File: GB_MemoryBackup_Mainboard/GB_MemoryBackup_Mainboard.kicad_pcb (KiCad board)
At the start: 2 copper layers, 56.5 x 64.4 mm, 18 parts, among them J1 GB_Cart_EdgeConn-1Row-32Pins, J2 GB_Cart_Slot-1Row-32Pins, J3 JTAG-A, SW1 SW_SPDT, SW2 SW_Push, U1 AT29C010A-PLCC32, U2 28SF040-120-4C-NH-PLCC32, U3 Generic-ATF15xx-PLCC44

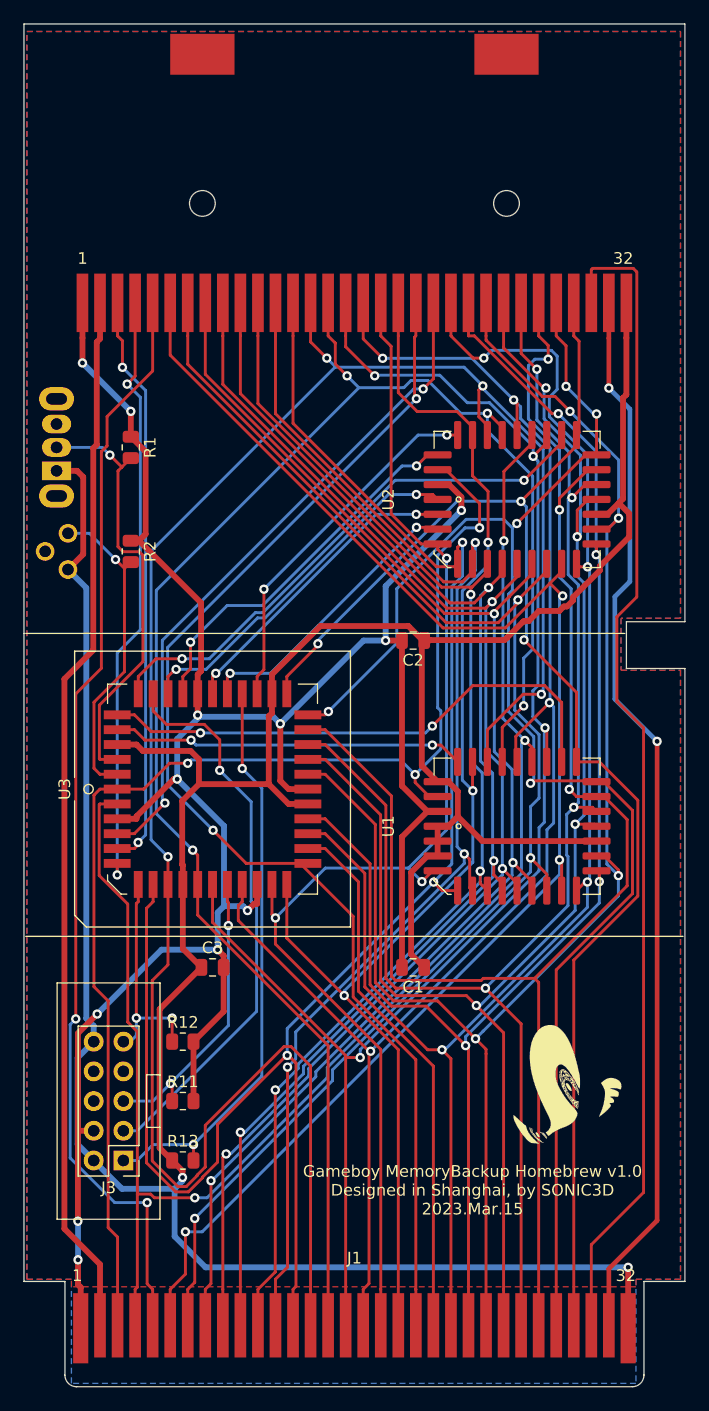
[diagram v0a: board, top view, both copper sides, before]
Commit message: Modified: PCB redesigned for using with plastic cart shell.
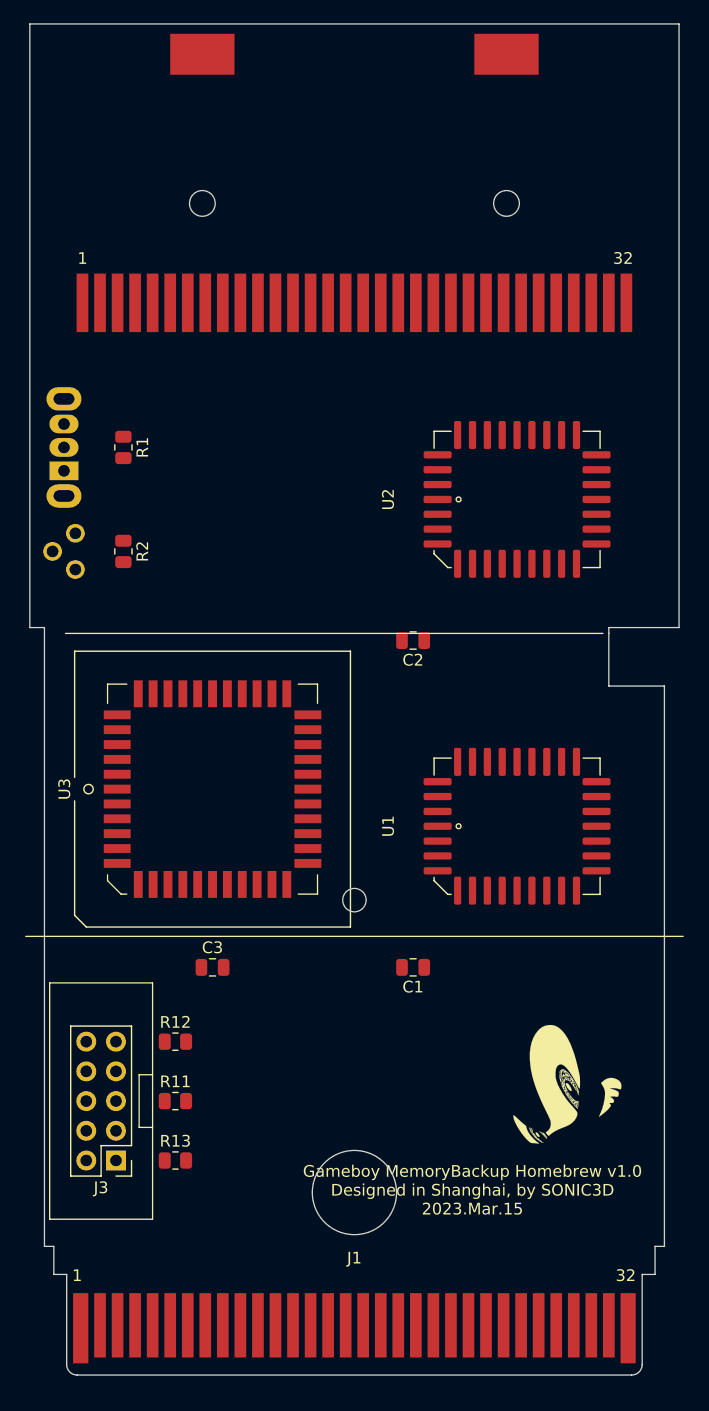
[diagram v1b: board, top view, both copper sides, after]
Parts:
- J1: footprint NintendoGBCart_ExtFootprint:GB_Cart_1x32_P1.50mm_Edge_For_RawPCB -> NintendoGBCart_ExtFootprint:GB_Cart_1x32_P1.50mm_Edge_For_CartShell
- moved R1 0.64 mm to (69.8, 76.2)
- moved R11 0.64 mm to (74.3, 132.1)
- moved R12 0.64 mm to (74.3, 127.0)
- moved R13 0.64 mm to (74.3, 137.2)
- moved R2 0.64 mm to (69.8, 85.1)
- moved J3 0.63 mm to (69.2, 137.2)
- moved SW1 0.63 mm to (64.8, 76.2)
- moved SW2 0.63 mm to (64.8, 85.1)
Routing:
- net GND: track 293.6 -> 0.00 mm, vias 2 -> 0
- net +5V: track 206.9 -> 0.00 mm, vias 12 -> 0
- net /AA8: track 181.4 -> 0.00 mm, vias 4 -> 0
- net /AA7: track 151.4 -> 0.00 mm, vias 3 -> 0
- net /AA9: track 149.1 -> 0.00 mm, vias 4 -> 0
- net /AD5: track 140.1 -> 0.00 mm, vias 3 -> 0
- net /AD2: track 135.7 -> 0.00 mm, vias 4 -> 0
- net /~ARD: track 133.9 -> 0.00 mm, vias 3 -> 0
- net /AA11: track 133.9 -> 0.00 mm, vias 4 -> 0
- net /AD3: track 133.3 -> 0.00 mm, vias 4 -> 0
- net /AA10: track 131.9 -> 0.00 mm, vias 4 -> 0
- net /AA0: track 131.6 -> 0.00 mm, vias 3 -> 0
- net /AD4: track 131.5 -> 0.00 mm, vias 4 -> 0
- net /AD6: track 131.3 -> 0.00 mm, vias 5 -> 0
- net /AD0: track 130.5 -> 0.00 mm, vias 4 -> 0
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- removed copper zone on F.Cu, net +5V
- removed copper zone on B.Cu, net GND
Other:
- board size 56.5 x 64.4 mm -> 55.5 x 104.5 mm

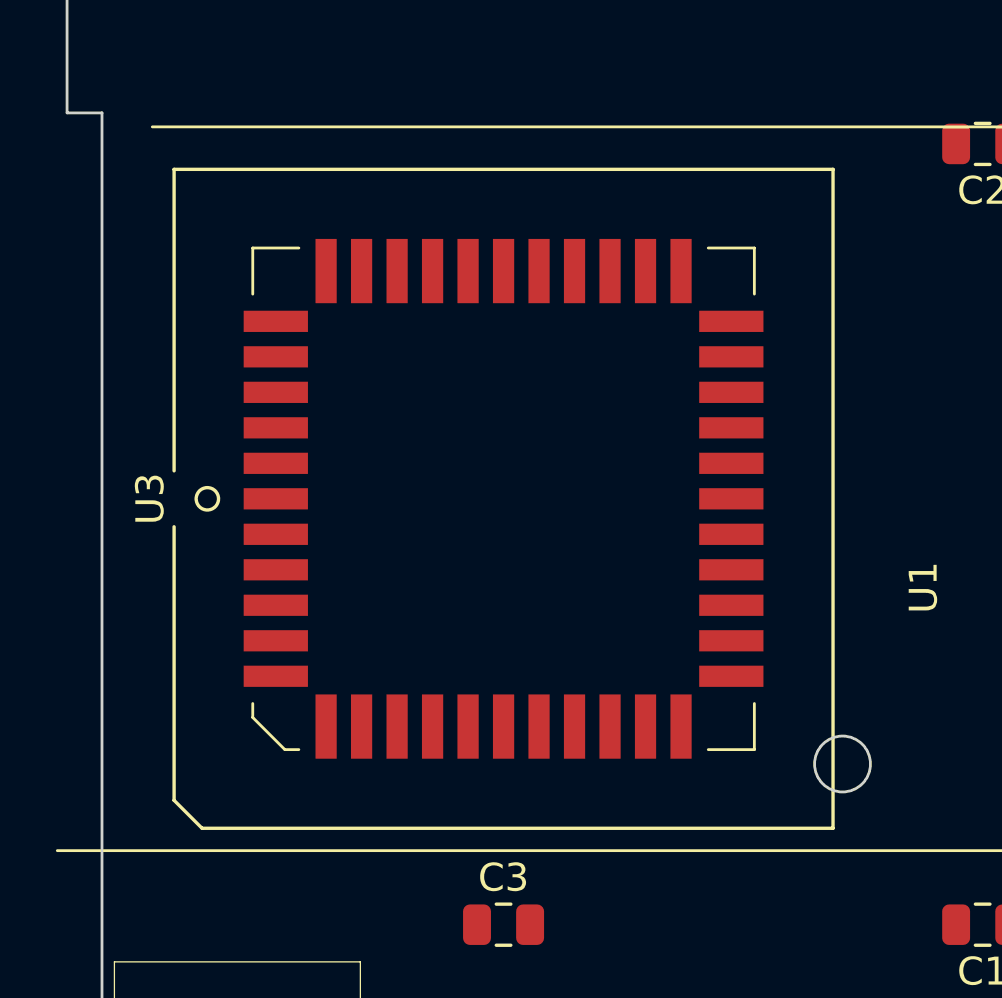
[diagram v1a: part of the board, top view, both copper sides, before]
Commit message: Modified: Moved PLCC-44 IC socket for the cartridge shell hole.
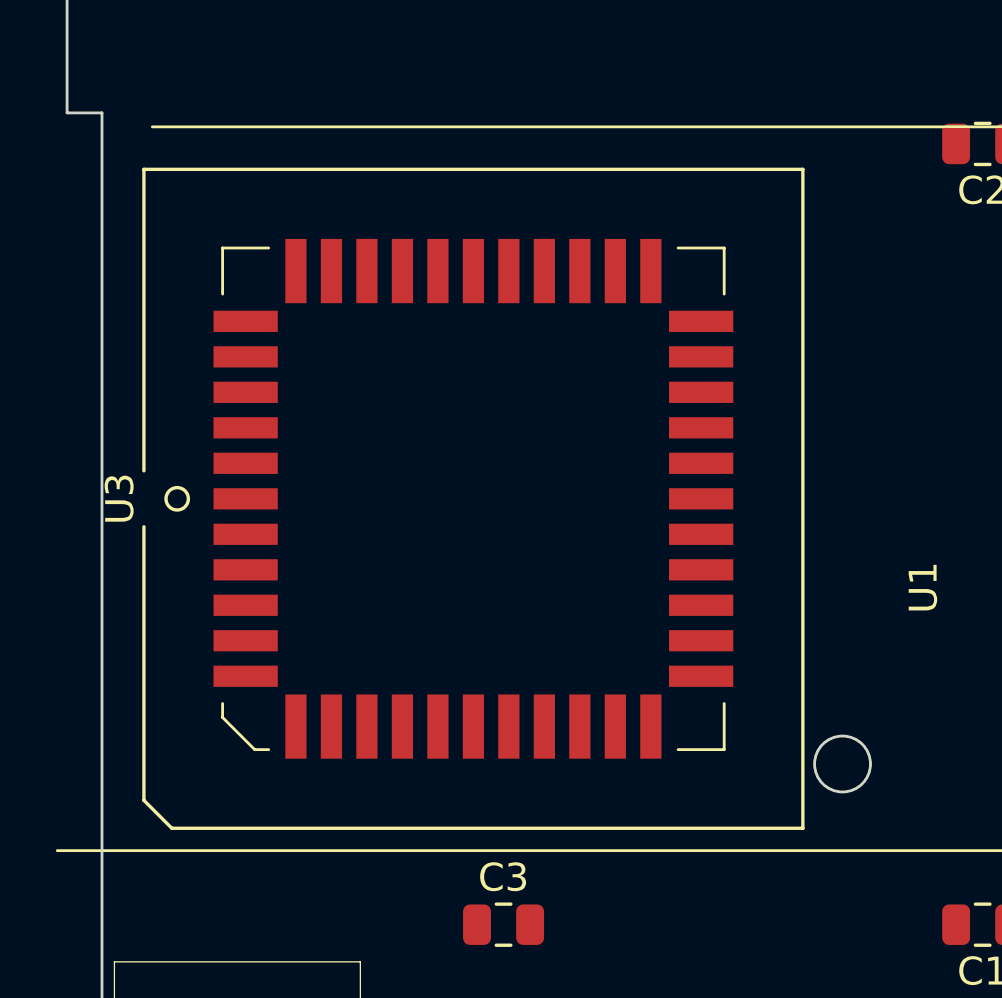
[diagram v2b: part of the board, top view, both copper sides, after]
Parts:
- moved U3 1.08 mm to (76.4, 105.4)

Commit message: Modified: Changed info text layer for auto routing.
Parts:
- removed the G*** at (68.6, 50.8)

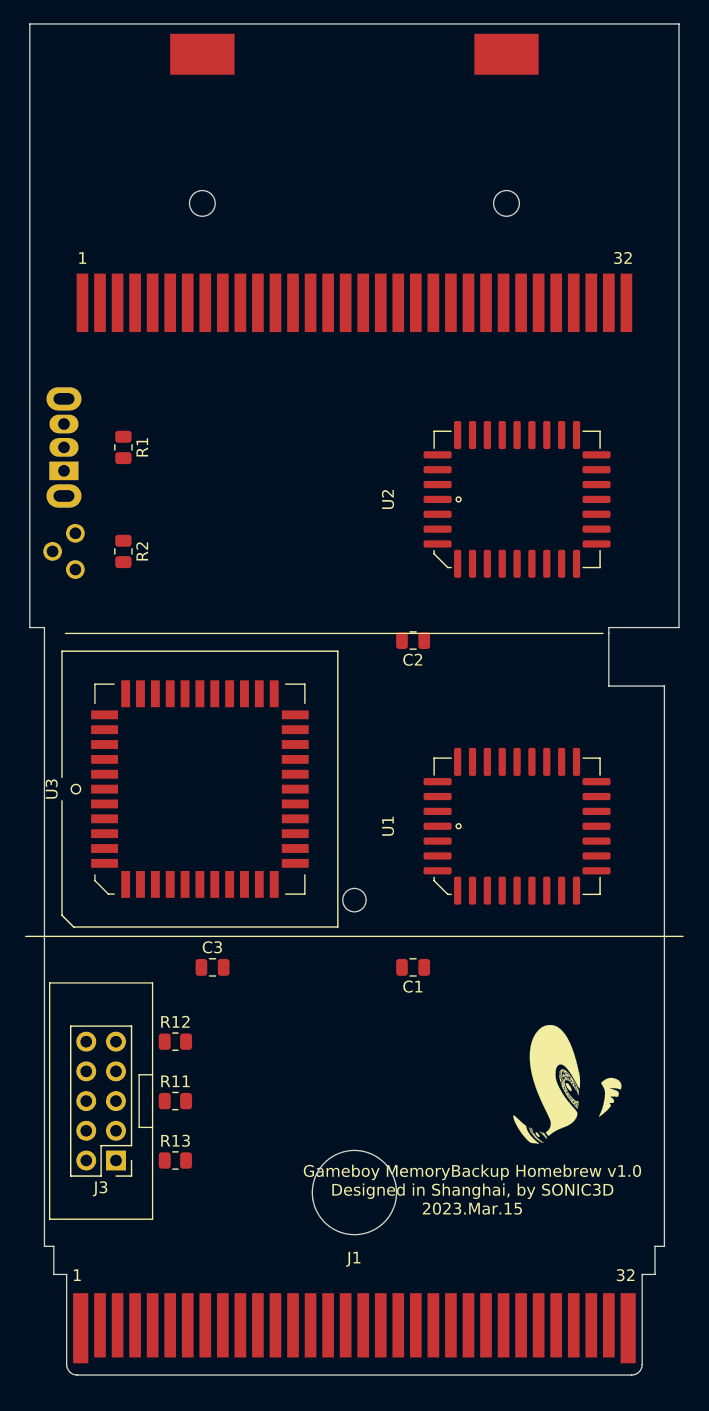
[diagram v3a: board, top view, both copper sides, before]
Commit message: Modified: Auto routed and manually revised.
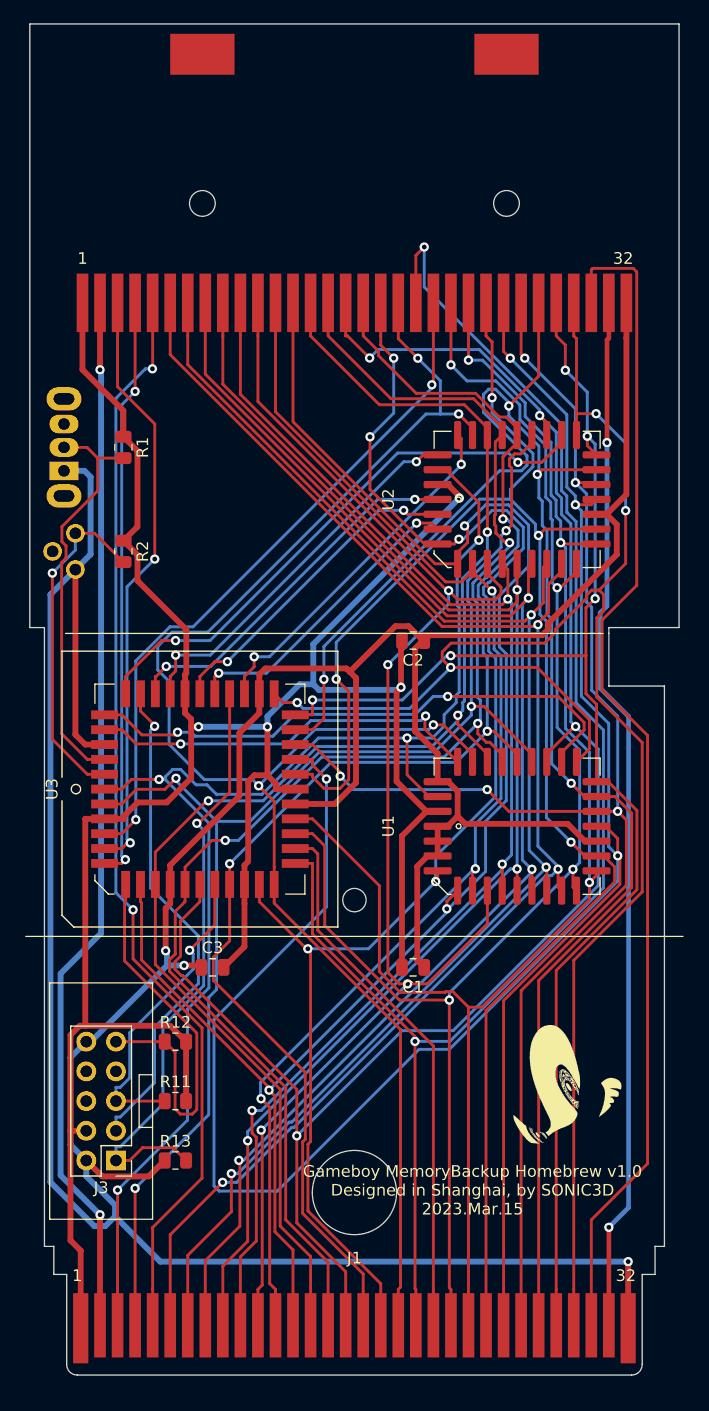
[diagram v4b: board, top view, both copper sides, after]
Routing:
- net GND: track 0.00 -> 326.7 mm, vias 0 -> 3
- net +5V: track 0.00 -> 217.2 mm, vias 0 -> 4
- net /AD3: track 0.00 -> 191.6 mm, vias 0 -> 4
- net /AA10: track 0.00 -> 150.7 mm, vias 0 -> 4
- net /AD7: track 0.00 -> 149.8 mm, vias 0 -> 4
- net /AD5: track 0.00 -> 146.5 mm, vias 0 -> 4
- net /AA7: track 0.00 -> 143.0 mm, vias 0 -> 3
- net /AD2: track 0.00 -> 141.9 mm, vias 0 -> 4
- net /AA13: track 0.00 -> 138.5 mm, vias 0 -> 4
- net /AA14: track 0.00 -> 132.4 mm, vias 0 -> 2
- net /AA0: track 0.00 -> 129.0 mm, vias 0 -> 3
- net /AA8: track 0.00 -> 128.9 mm, vias 0 -> 3
- net /AA9: track 0.00 -> 128.7 mm, vias 0 -> 3
- net /AD1: track 0.00 -> 127.5 mm, vias 0 -> 3
- net /AD4: track 0.00 -> 126.9 mm, vias 0 -> 5
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
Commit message: Modified: Added copper filled zone. Modified: PCB version updated to v1.1.
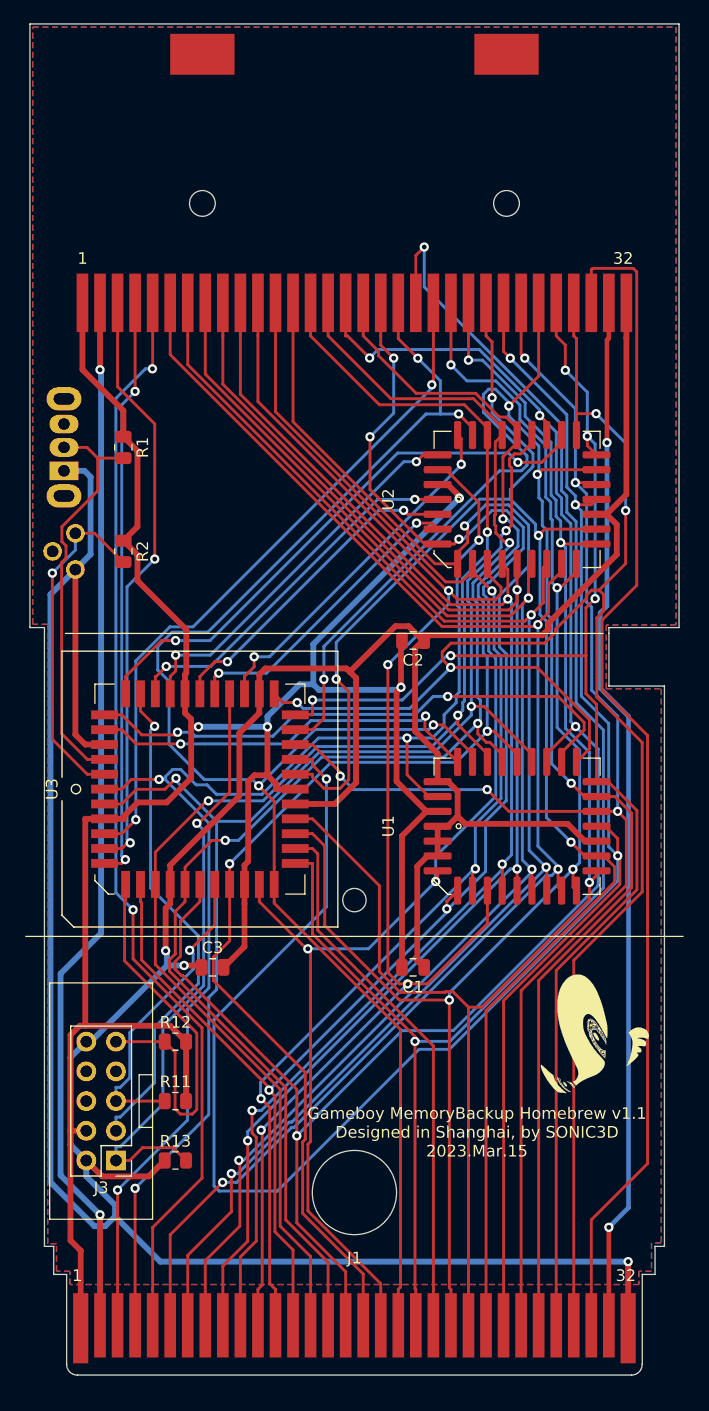
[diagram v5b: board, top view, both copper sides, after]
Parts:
- added G***: LOGO, LogoGraphics:MaskLayer_12mm_x_12mm_ShadowSonic, B.Cu at (68.5, 50.8)
- moved G*** 4.92 mm to (110.3, 126.5)
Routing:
- added copper zone on F.Cu, net +5V
- added copper zone on B.Cu, net GND
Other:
- board text added: "Gameboy MemoryBackup Homebrew v1.1 Designed in Shanghai, by SONIC3D 2023.Mar.15"
- board text added: "Gameboy MemoryBackup Homebrew v1.1 https://github.com/SONIC3D/gameboy-memorybackup Designed in Shanghai, by SONIC3D 2023.Mar.15"
- board text removed: "Gameboy MemoryBackup Homebrew v1.0 Designed in Shanghai, by SONIC3D 2023.Mar.15"
- board text removed: "Gameboy MemoryBackup Homebrew v1.0 https://github.com/SONIC3D/gameboy-memorybackup Designed in Shanghai, by SONIC3D 2023.Mar.15"
